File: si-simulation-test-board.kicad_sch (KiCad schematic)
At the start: 27 parts, among them J1 Conn_SMA_RF2-143-T-17-50-G, J10 Conn_SMA_RF2-143-T-17-50-G, J11 Conn_SMA_RF2-143-T-17-50-G, J12 Conn_SMA_RF2-143-T-17-50-G, J13 Conn_SMA_RF2-143-T-17-50-G, J14 Conn_SMA_RF2-143-T-17-50-G, J15 Conn_SMA_RF2-143-T-17-50-G, J16 Conn_SMA_RF2-143-T-17-50-G, J17 Conn_SMA_RF2-143-T-17-50-G, J18 Conn_SMA_RF2-143-T-17-50-G, J19 Conn_SMA_RF2-143-T-17-50-G, J2 Conn_SMA_RF2-143-T-17-50-G, J20 Conn_SMA_RF2-143-T-17-50-G, J21 Conn_SMA_RF2-143-T-17-50-G, J22 Conn_SMA_RF2-143-T-17-50-G, J3 Conn_SMA_RF2-143-T-17-50-G, J4 Conn_SMA_RF2-143-T-17-50-G, J5 Conn_SMA_RF2-143-T-17-50-G, J6 Conn_SMA_RF2-143-T-17-50-G, J7 Conn_SMA_RF2-143-T-17-50-G, J8 Conn_SMA_RF2-143-T-17-50-G, J9 Conn_SMA_RF2-143-T-17-50-G

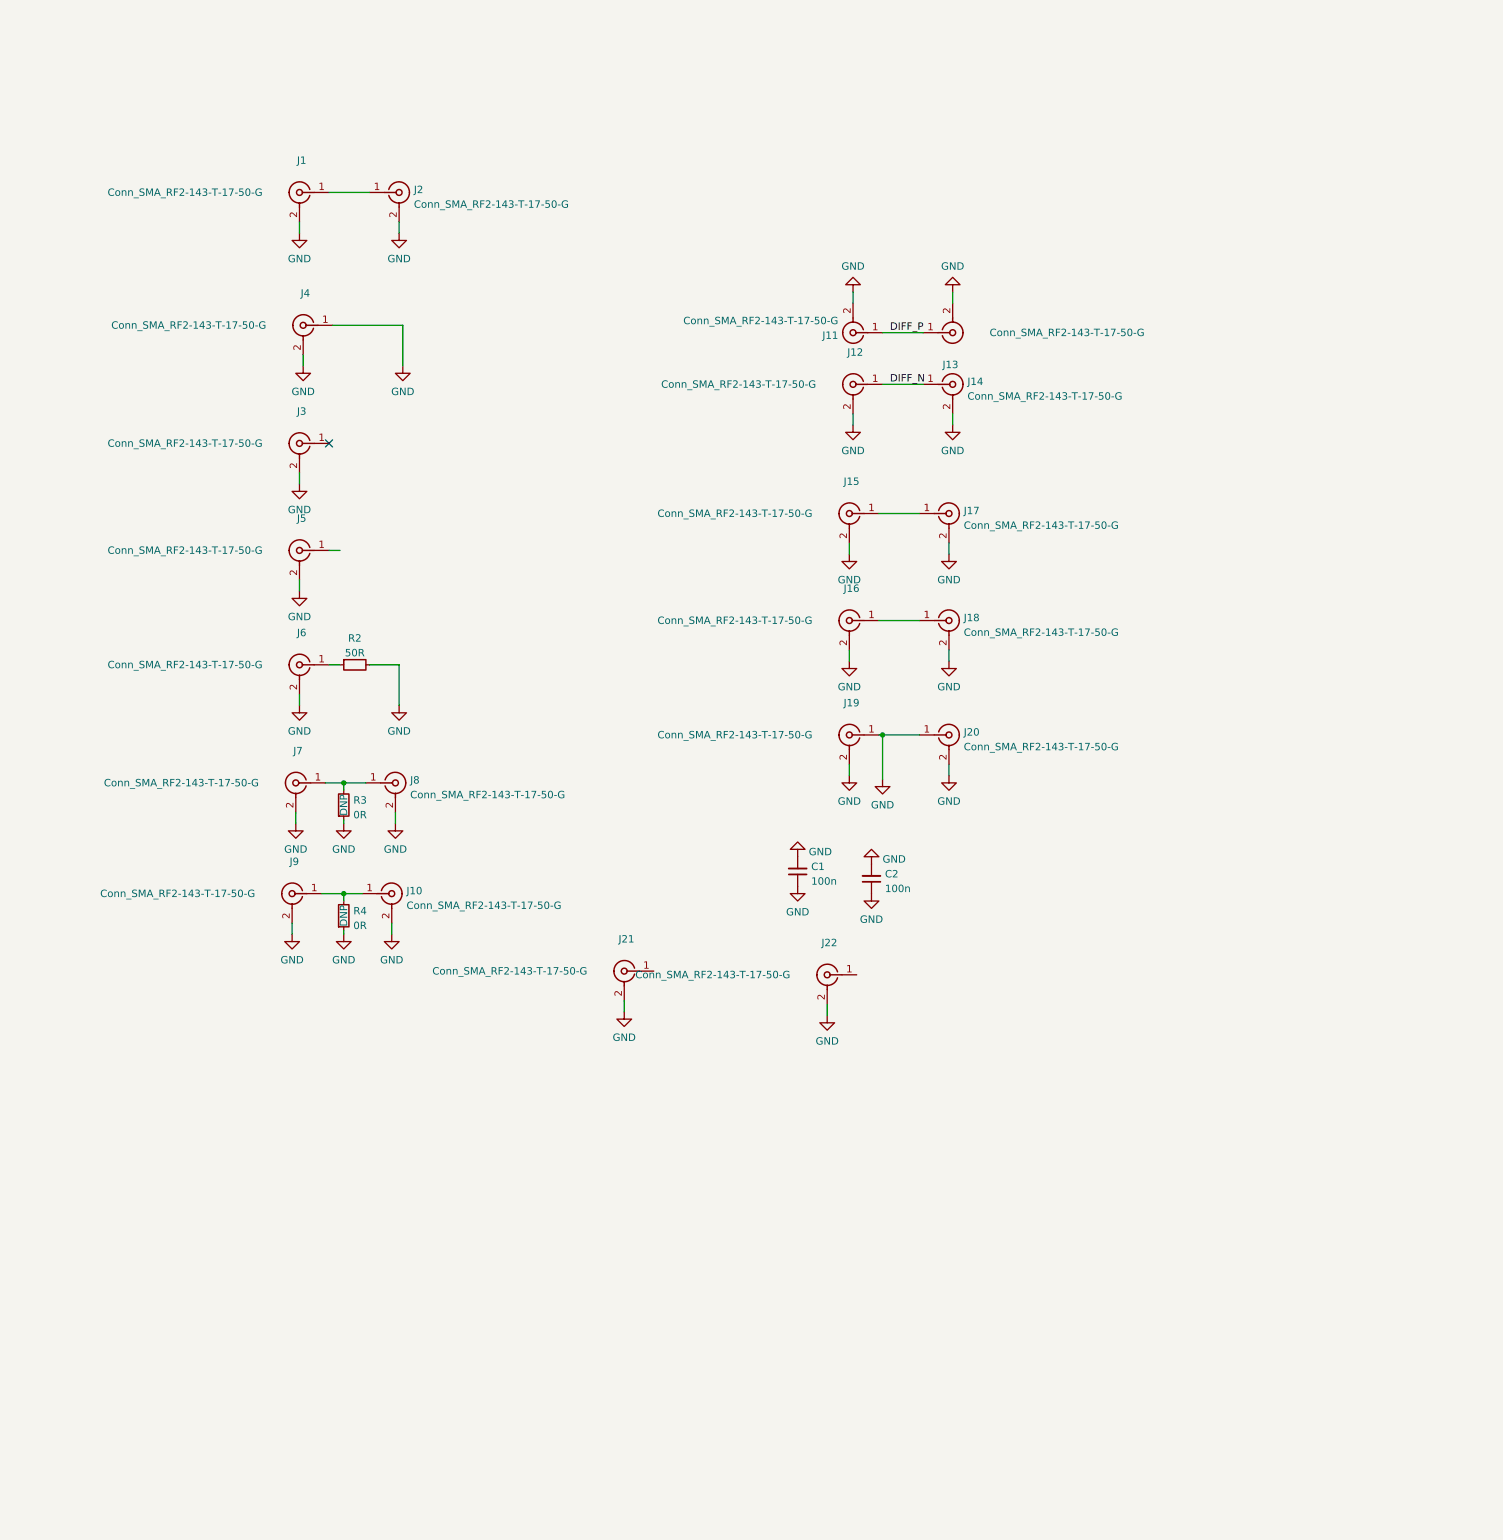
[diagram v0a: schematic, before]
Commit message: Improve schematic clarity
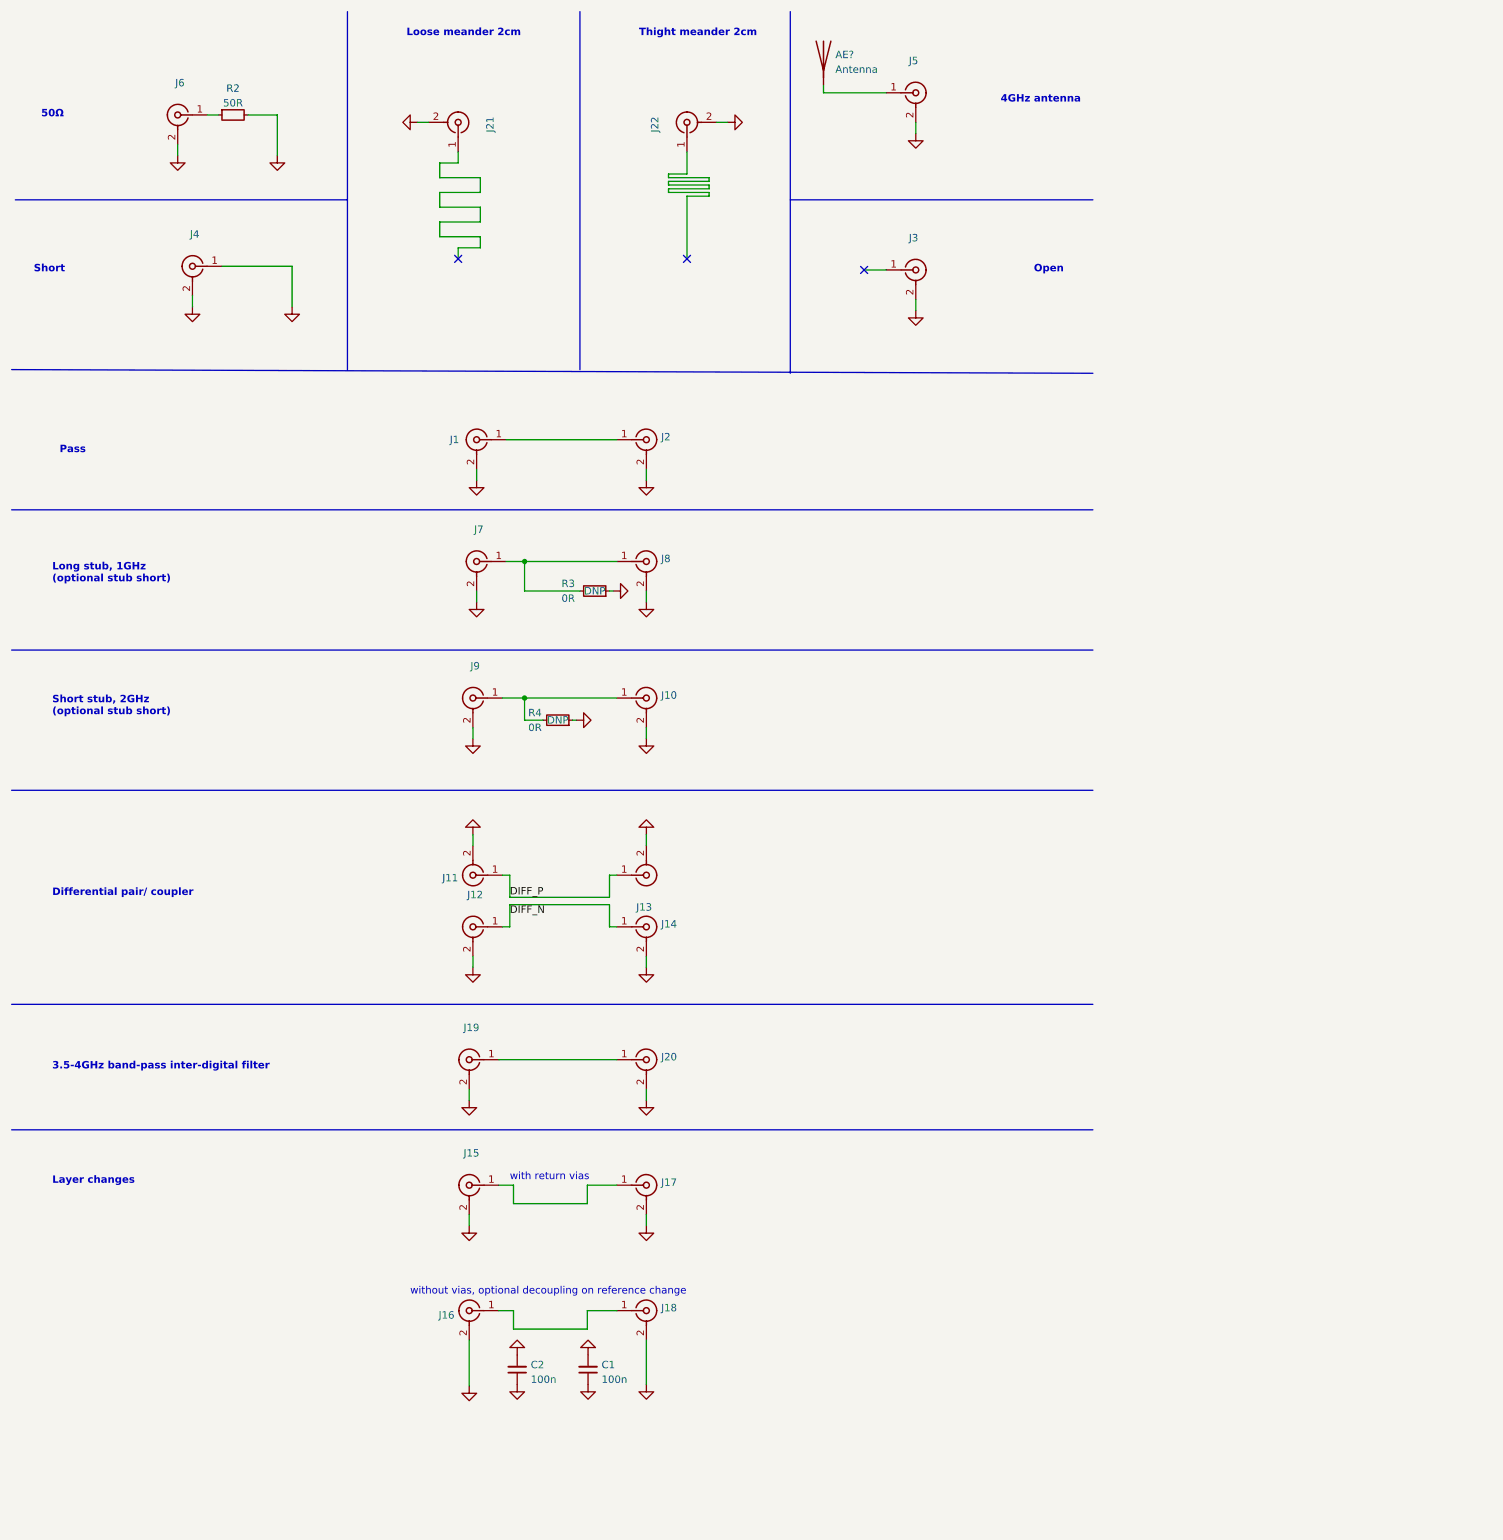
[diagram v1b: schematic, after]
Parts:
- added AE?: Antenna, symbol Device:Antenna
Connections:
- net GND: no longer J19.1, J20.1
- net at J5.1: now also AE?.1 (A)
- new net: J19.1, J20.1
- no-connect marks 1 -> 3
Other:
- note added: "3.5-4GHz band-pass inter-digital filter"
- note added: "4GHz antenna"
- note added: "50Ω"
- note added: "Differential pair/ coupler"
- note added: "Layer changes"
- note added: "Long stub, 1GHz (optional stub short)"
- note added: "Loose meander 2cm"
- note added: "Open"
- note added: "Pass"
- note added: "Short"
- note added: "Short stub, 2GHz (optional stub short)"
- note added: "Thight meander 2cm"
- note added: "with return vias"
- note added: "without vias, optional decoupling on reference change"
- title: (none) -> SI test board
- moved on the sheet: C1, C2, J1, J10, J11, J12, J13, J14, J15, J16, J17, J18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

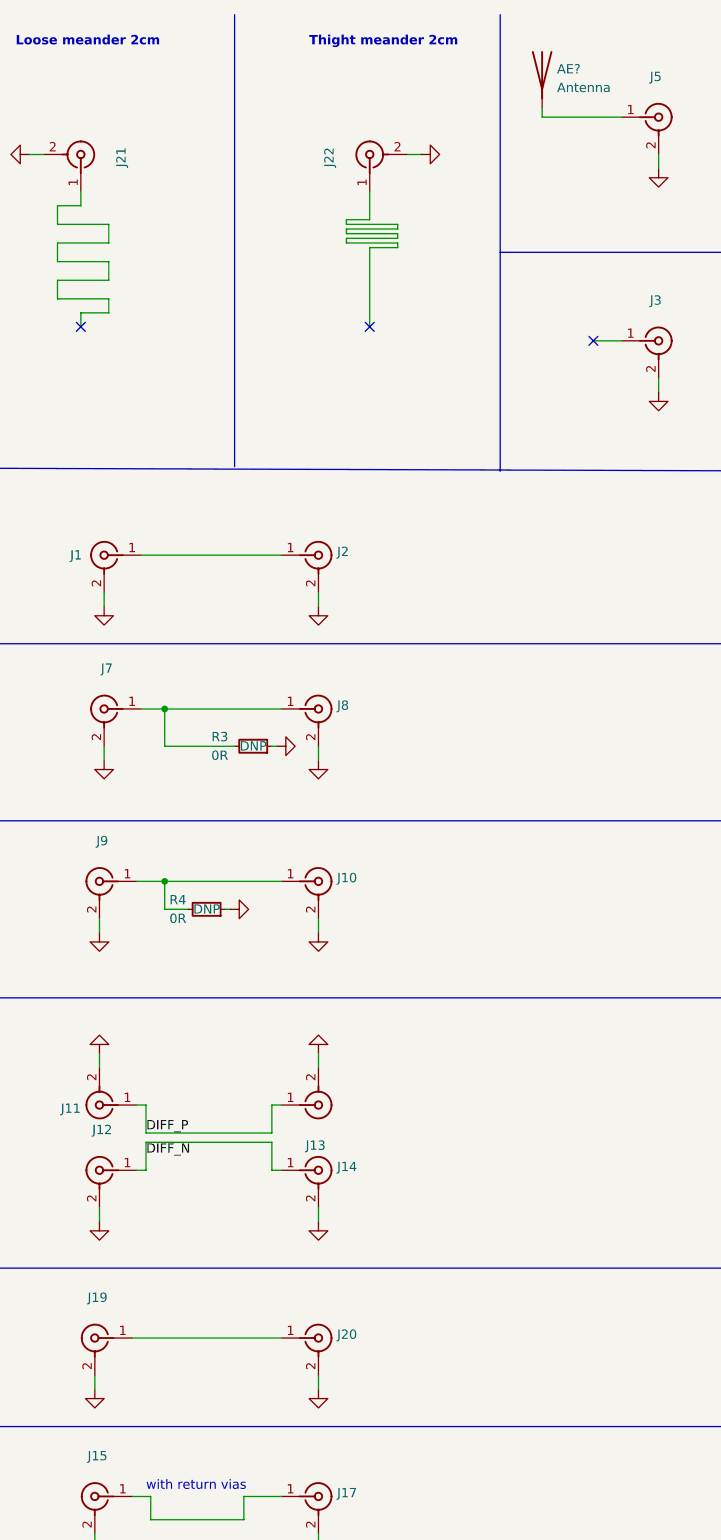
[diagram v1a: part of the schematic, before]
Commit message: Clean DRC, add missing cutouts for upper connectors, fix antenna feed point, standarize footprint, bump to 1.0.1
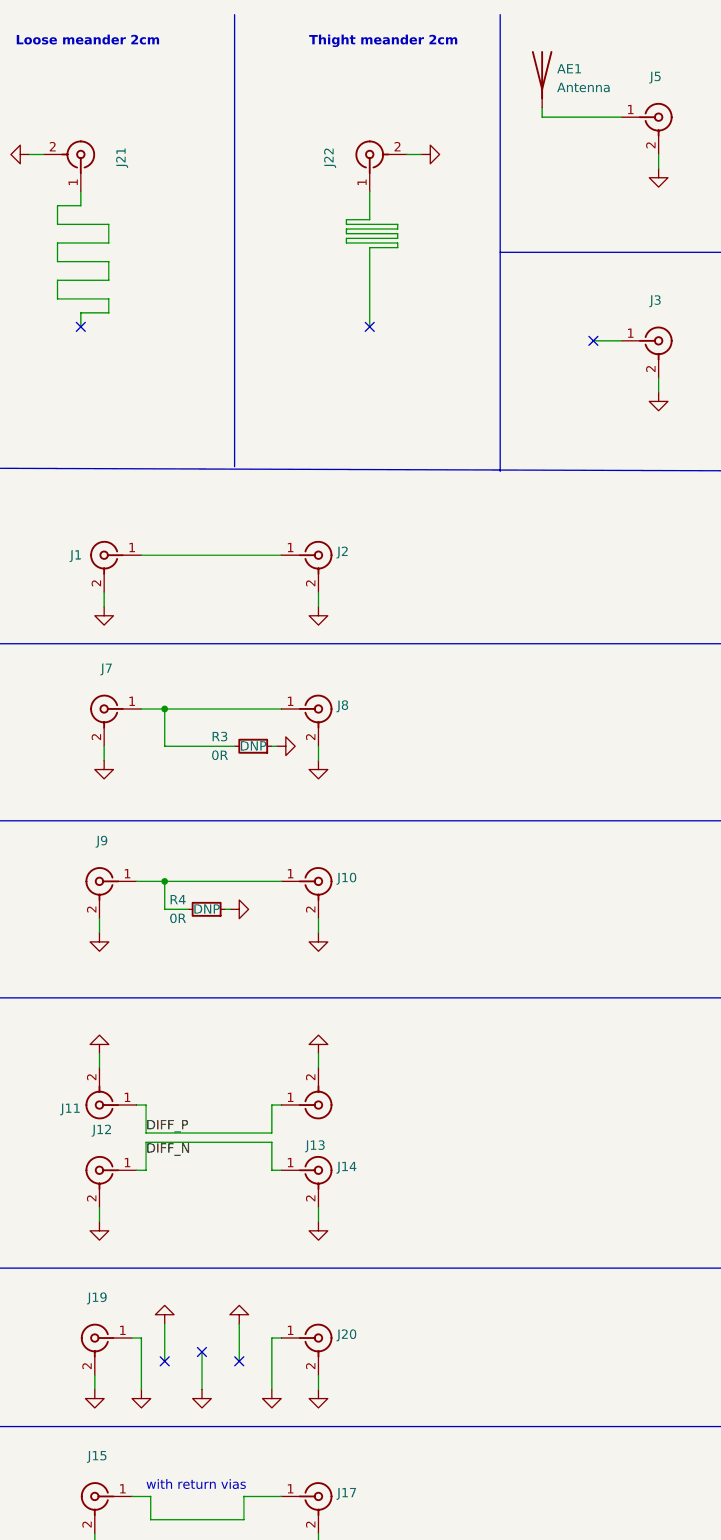
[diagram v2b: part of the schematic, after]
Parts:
- gave numbers to parts that had none: 1
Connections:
- net GND: now also J19.1, J20.1
- no-connect marks 3 -> 6
